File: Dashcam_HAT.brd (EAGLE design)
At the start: 65 x 56 mm, 73 parts, among them J1 RJ45-8PTH, J2 JST_VERTICAL, J3 PIN20X2, J5 M4, J7 6_PIN_SMD, Q1 MMBT2222, Q2 MMBT2222, U1 STN1110, U2 MCP2551, U3 TS30011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

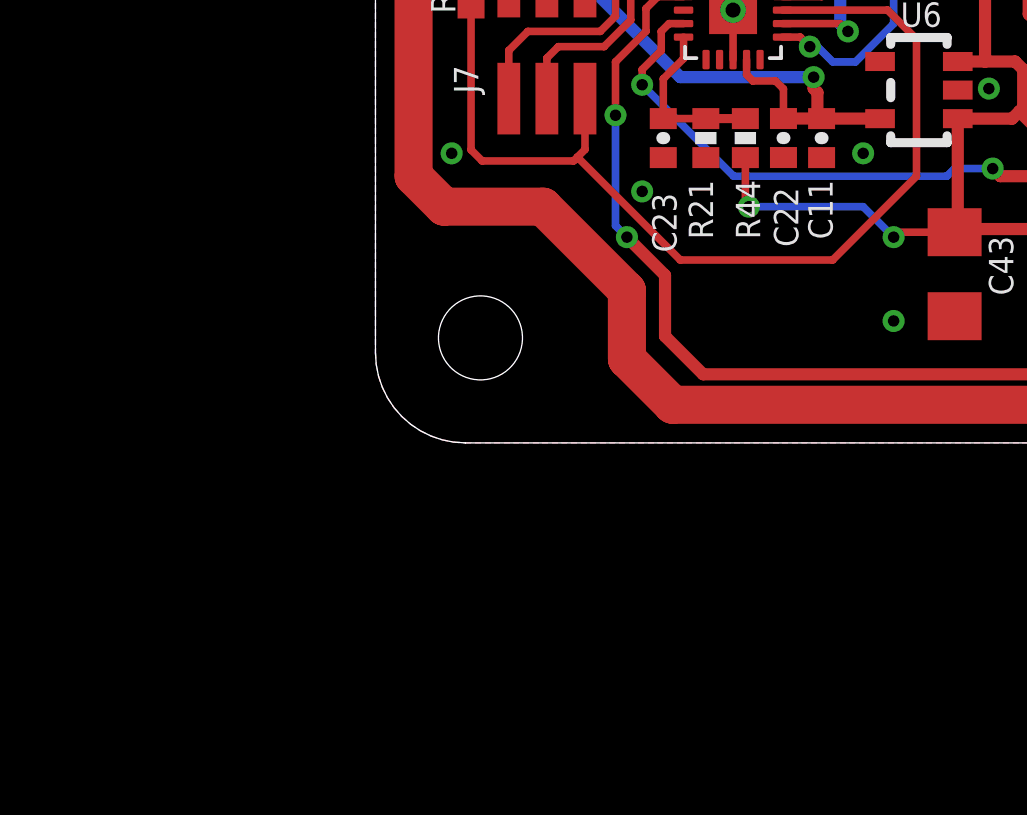
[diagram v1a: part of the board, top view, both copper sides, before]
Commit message: Updated part identifiers
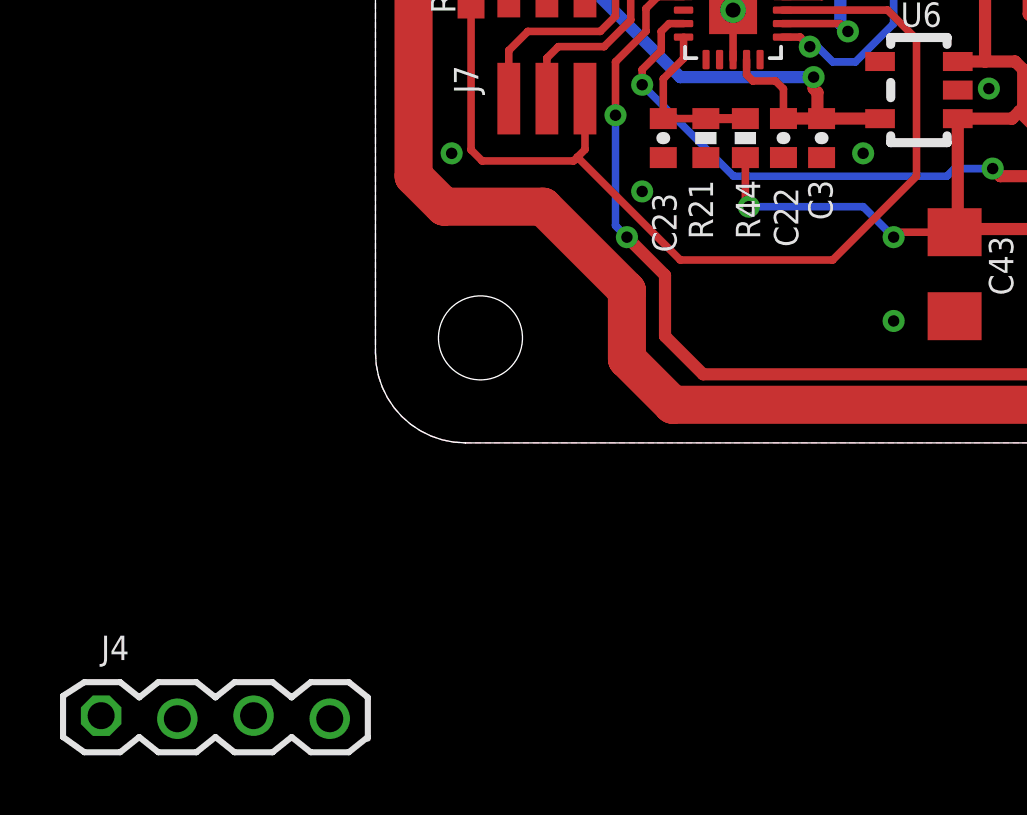
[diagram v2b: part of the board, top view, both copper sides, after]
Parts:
- added J4: M4, Jason_Connector:M4X1_LOCK
- renumbered C11 to C3
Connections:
- new net UART1_RX: J3.10
- new net UART1_TX: J3.8
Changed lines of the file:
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@@
 <attribute name="VALUE" x="17.781" y="7.02" size="0.4064" layer="27" rot="R270"/>
 </element>
-<element name="C11" library="SparkFun" package="0402-CAP" value="1uF" x="14.871" y="10.16" smashed="yes" rot="R270">
+<element name="C3" library="SparkFun" package="0402-CAP" value="1uF" x="14.871" y="10.16" smashed="yes" rot="R270">
 <attribute name="MANUFACTURER" value="Murata" x="14.871" y="10.16" size="1.778" layer="27" rot="R270" display="off"/>
 <attribute name="DIGIKEY_PN" value="490-3890-1-ND" x="14.871" y="10.16" size="1.778" layer="27" rot="R270" display="off"/>
@@
 <attribute name="VALUE" x="18.669" y="46.6725" size="0.4064" layer="27" rot="R90"/>
 </element>
+<element name="J4" library="Jason_Connector" package="M4X1_LOCK" value="M4" x="-9.144" y="-9.144"/>
 </elements>
 <signals>
@@
 <contactref element="C40" pad="2"/>
 <contactref element="C43" pad="2"/>
-<contactref element="C11" pad="2"/>
+<contactref element="C3" pad="2"/>
 <contactref element="C41" pad="2"/>
 <contactref element="C42" pad="2"/>
@@
 <signal name="VCC-AVR">
 <contactref element="U6" pad="5"/>
-<contactref element="C11" pad="1"/>
+<contactref element="C3" pad="1"/>
 <contactref element="U4" pad="9"/>
 <contactref element="C22" pad="1"/>
@@
 <wire x1="34.544" y1="45.466" x2="33.782" y2="46.228" width="0.3048" layer="16"/>
 </signal>
+<signal name="UART1_TX">
+<contactref element="J3" pad="8"/>
+</signal>
+<signal name="UART1_RX">
+<contactref element="J3" pad="10"/>
+</signal>
 </signals>

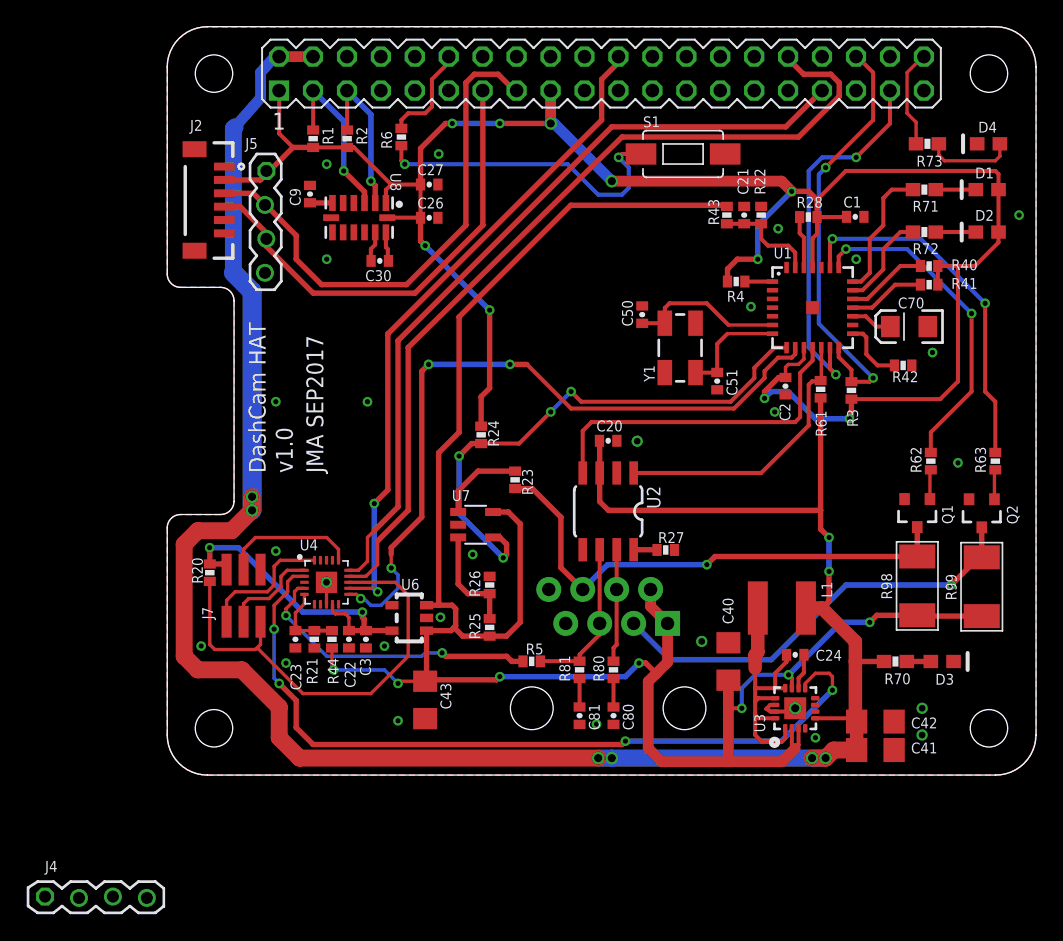
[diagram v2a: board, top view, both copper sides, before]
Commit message: Tweaked layout a bit and added more bypass caps
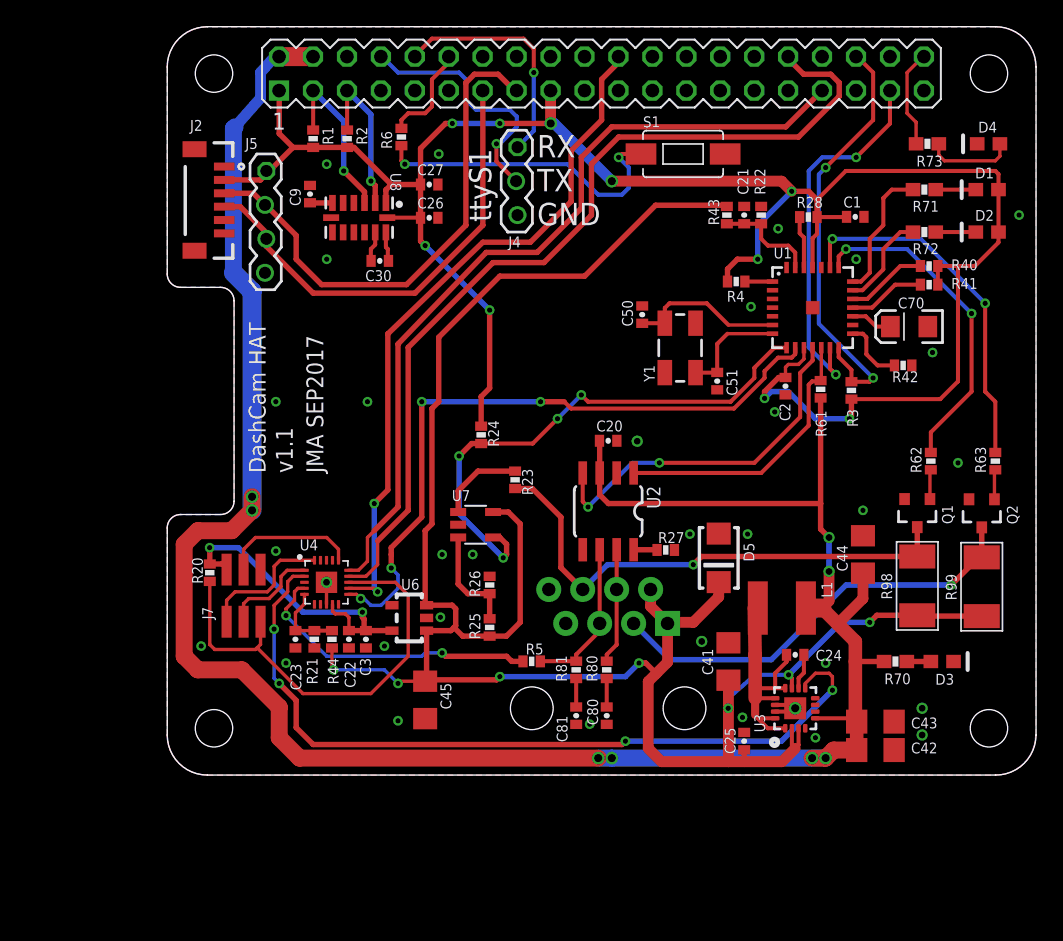
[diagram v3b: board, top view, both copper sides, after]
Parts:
- removed C40: 10uF, SparkFun-Capacitors:1206
- added C25: 0.1uF, SparkFun:0402-CAP
- added C44, C45: 10uF, SparkFun-Capacitors:1206
- added D5: SMAJ16A, Jason_Library_1:SMA
- J4: value M4 -> (none); device Jason_Connector:M4X1_LOCK -> Jason_Connector:M3X1_LOCK
- moved J4 66.3 mm to (26.2, 47.0), turned to 270 degrees
- moved C43 33.7 mm to (53.0, 4.00), turned to 0 degrees
- moved C41 12.8 mm to (42.0, 8.50), turned to 90 degrees
- moved C42 2.13 mm to (53.0, 1.87)
- moved C80 0.51 mm to (32.9, 4.45)
- moved R80 0.51 mm to (32.9, 7.87)
- moved C81 0.25 mm to (30.6, 4.45)
- moved R81 0.25 mm to (30.6, 7.87)
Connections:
- net N$16 renamed VSW
- net N$19 renamed BST
- net 5V: now also C43.1, C44.1; no longer C41.1
- net GND: now also C25.1, C44.2, C45.2, D5.A, J4.3; no longer C40.2
- net UART1_RX: now also J4.1
- net UART1_TX: now also J4.2
- net VBATT: now also C25.2, C41.1, C45.1, D5.K; no longer C40.1, C43.1
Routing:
- net UART1_TX: track 0.00 -> 19.1 mm, vias 0 -> 1
- net UART1_RX: track 0.00 -> 17.7 mm, vias 0 -> 1
- net VBATT: track 155.9 -> 162.6 mm
- net 5V: track 166.0 -> 170.1 mm
- net !STN_SLEEP: track 54.0 -> 50.3 mm
- net AVR_RX: track 65.5 -> 67.8 mm
- net AVR_TX: track 58.6 -> 60.8 mm
- net SHUTDOWN: track 50.0 -> 52.2 mm
- net VSW: track 21.2 -> 19.2 mm
- net CAN_RX: track 25.4 -> 26.9 mm, vias 0 -> 2
- net GND: track 4.77 -> 4.86 mm, vias 27 -> 33
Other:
- board text added: "GND"
- board text added: "RX"
- board text added: "TX"
- board text added: "ttyS1"
- board text added: "v1.1"
- board text removed: "v1.0"

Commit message: tweaked layout
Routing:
- net 5V: track 170.1 -> 180.9 mm, vias 8 -> 9
- net 3.3V: track 159.5 -> 162.0 mm
- net GND: vias 33 -> 34
- added copper zone on layer 1, net 5V
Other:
- board text added: "3.3V"
- board text added: "5V"
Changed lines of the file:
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@@
 <text x="27.686" y="41.148" size="1.6764" layer="25" ratio="12">GND</text>
 <text x="24.257" y="41.402" size="1.6764" layer="25" ratio="12" rot="R90">ttyS1</text>
+<text x="7.112" y="19.05" size="1.27" layer="21" ratio="12" rot="SR0">5V</text>
+<text x="11.684" y="19.05" size="1.27" layer="21" ratio="12" rot="SR0">3.3V</text>
 </plain>
 <attributes>
@@
 <contactref element="J3" pad="30"/>
 <contactref element="J3" pad="34"/>
-<polygon width="0.254" layer="16" isolate="0.254">
+<polygon width="0.254" layer="16" isolate="0.254" rank="6">
 <vertex x="0" y="3" curve="90"/>
 <vertex x="3" y="0"/>
@@
 <vertex x="0" y="18.5"/>
 </polygon>
-<polygon width="0.254" layer="1" isolate="0.254">
+<polygon width="0.254" layer="1" isolate="0.254" rank="6">
 <vertex x="0" y="3" curve="90"/>
 <vertex x="3" y="0"/>
@@
 <via x="20.574" y="16.51" extent="1-16" drill="0.381"/>
 <contactref element="C25" pad="1"/>
+<via x="5.334" y="48.006" extent="1-16" drill="0.381"/>
 </signal>
 <signal name="SCL1">
@@
 <contactref element="J3" pad="1"/>
 <contactref element="J3" pad="17"/>
-<wire x1="9.413" y1="46.975" x2="8.382" y2="48.006" width="0.4064" layer="1"/>
-<wire x1="8.382" y1="48.006" x2="8.382" y2="51.218" width="0.4064" layer="1"/>
-<wire x1="8.382" y1="51.218" x2="8.37" y2="51.23" width="0.3048" layer="1"/>
 <contactref element="R1" pad="2"/>
 <contactref element="R2" pad="2"/>
@@
 <wire x1="46.272" y1="29.754" x2="45.756" y2="29.754" width="0.4064" layer="1"/>
 <wire x1="45.756" y1="29.754" x2="44.704" y2="28.702" width="0.4064" layer="1"/>
+<wire x1="8.37" y1="51.23" x2="8.304" y2="51.23" width="0.4064" layer="1"/>
+<wire x1="8.304" y1="51.23" x2="6.604" y2="49.53" width="0.4064" layer="1"/>
+<wire x1="6.604" y1="49.53" x2="6.604" y2="46.0248" width="0.4064" layer="1"/>
+<wire x1="6.604" y1="46.0248" x2="7.4168" y2="45.212" width="0.4064" layer="1"/>
 </signal>
 <signal name="N$35">
@@
 <wire x1="51.35" y1="4.25" x2="51.6" y2="4" width="0.3048" layer="1"/>
 <wire x1="53.65" y1="8.5" x2="51.5" y2="8.5" width="0.4064" layer="1"/>
-<wire x1="10.91" y1="53.77" x2="8.37" y2="53.77" width="1.4224" layer="1"/>
-<wire x1="8.37" y1="53.77" x2="8.05" y2="53.77" width="0.8128" layer="16"/>
-<wire x1="8.05" y1="53.77" x2="6.985" y2="52.578" width="0.8128" layer="16"/>
-<wire x1="4.953" y1="37.592" x2="6.35" y2="36.195" width="1.4224" layer="16"/>
-<wire x1="6.35" y1="36.195" x2="6.35" y2="19.812" width="1.4224" layer="16"/>
+<wire x1="6.35" y1="34.036" x2="6.35" y2="19.812" width="1.4224" layer="16"/>
 <contactref element="R61" pad="1"/>
 <via x="33.274" y="1.27" extent="1-16" drill="0.6"/>
@@
 <via x="6.35" y="20.828" extent="1-16" drill="0.6"/>
 <wire x1="6.35" y1="19.812" x2="6.35" y2="20.828" width="1.27" layer="1"/>
-<wire x1="6.985" y1="52.578" x2="6.985" y2="50.673" width="0.8128" layer="16"/>
-<wire x1="6.985" y1="50.673" x2="5.08" y2="48.514" width="0.8128" layer="16"/>
-<wire x1="4.953" y1="37.592" x2="4.953" y2="48.387" width="1.27" layer="16"/>
-<wire x1="4.953" y1="48.387" x2="5.08" y2="48.514" width="1.27" layer="16"/>
 <via x="49.276" y="1.27" extent="1-16" drill="0.6"/>
 <wire x1="49.879" y1="1.873" x2="49.276" y2="1.27" width="1.27" layer="1"/>
@@
 <wire x1="49.53" y1="15.24" x2="49.53" y2="13.03" width="0.8128" layer="1"/>
 <wire x1="49.53" y1="13.03" x2="49" y2="12.5" width="0.8128" layer="1"/>
+<wire x1="6.35" y1="34.036" x2="9.652" y2="37.338" width="1.4224" layer="16"/>
+<wire x1="9.652" y1="37.338" x2="9.652" y2="47.244" width="1.4224" layer="16"/>
+<wire x1="9.652" y1="47.244" x2="8.509" y2="48.387" width="1.4224" layer="16"/>
+<wire x1="8.37" y1="53.77" x2="8.304" y2="53.77" width="0.4064" layer="16"/>
+<wire x1="8.304" y1="53.77" x2="7.112" y2="52.578" width="0.4064" layer="16"/>
+<wire x1="7.112" y1="52.578" x2="7.112" y2="49.784" width="0.4064" layer="16"/>
+<wire x1="7.112" y1="49.784" x2="8.255" y2="48.641" width="0.4064" layer="16"/>
+<wire x1="8.255" y1="48.641" x2="8.382" y2="48.514" width="0.4064" layer="16"/>
+<wire x1="8.382" y1="48.514" x2="8.509" y2="48.387" width="0.4064" layer="16"/>
+<wire x1="9.652" y1="52.07" x2="9.652" y2="50.038" width="0.4064" layer="16"/>
+<wire x1="9.652" y1="50.038" x2="8.255" y2="48.641" width="0.4064" layer="16"/>
+<via x="8.382" y="48.514" extent="1-16" drill="0.6"/>
+<wire x1="9.652" y1="50.038" x2="8.255" y2="48.641" width="0.4064" layer="1"/>
+<wire x1="9.652" y1="52.07" x2="9.652" y2="50.038" width="0.4064" layer="1"/>
+<wire x1="10.91" y1="53.328" x2="9.652" y2="52.07" width="0.4064" layer="1"/>
+<wire x1="10.91" y1="53.77" x2="10.91" y2="53.328" width="0.4064" layer="1"/>
+<wire x1="10.91" y1="53.328" x2="9.652" y2="52.07" width="0.4064" layer="16"/>
+<wire x1="10.91" y1="53.77" x2="10.91" y2="53.328" width="0.4064" layer="16"/>
+<polygon width="0.4064" layer="1" isolate="0.254" orphans="yes">
+<vertex x="6.985" y="55.118"/>
+<vertex x="6.985" y="52.324"/>
+<vertex x="11.557" y="52.324"/>
+<vertex x="11.557" y="55.118"/>
+</polygon>
 </signal>
 <signal name="N$11">
@@
 <wire x1="33.77" y1="53.328" x2="32.512" y2="52.07" width="0.4064" layer="1"/>
 <wire x1="32.512" y1="52.07" x2="32.512" y2="49.022" width="0.4064" layer="1"/>
-<wire x1="16.51" y1="33.02" x2="16.51" y2="21.336" width="0.4064" layer="1"/>
-<wire x1="16.51" y1="21.336" x2="15.494" y2="20.32" width="0.4064" layer="1"/>
+<wire x1="16.51" y1="33.02" x2="16.51" y2="21.59" width="0.4064" layer="1"/>
+<wire x1="16.51" y1="21.59" x2="15.494" y2="20.574" width="0.4064" layer="1"/>
 <via x="15.748" y="13.716" extent="1-16" drill="0.381"/>
-<via x="15.494" y="20.32" extent="1-16" drill="0.381"/>
-<wire x1="15.494" y1="20.32" x2="15.494" y2="13.97" width="0.4064" layer="16"/>
+<via x="15.494" y="20.574" extent="1-16" drill="0.381"/>
+<wire x1="15.494" y1="20.574" x2="15.494" y2="13.97" width="0.4064" layer="16"/>
 <wire x1="15.494" y1="13.97" x2="15.748" y2="13.716" width="0.4064" layer="16"/>
 <wire x1="13.57" y1="13.976" x2="15.488" y2="13.976" width="0.254" layer="1"/>
@@
 <wire x1="27.432" y1="48.2092" x2="26.2128" y2="46.99" width="0.3048" layer="16"/>
 </signal>
+<signal name="N$16">
+<via x="10.922" y="19.812" extent="1-16" drill="0.6"/>
+</signal>
 </signals>
